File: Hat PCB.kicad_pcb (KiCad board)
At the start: 2 copper layers, 35 x 23 mm, 21 parts, among them J1 Batt, J2 Input 1, J3 USB4125-GF-A_REVA2, J4 ICSP, J5 Motor, Q1 AO3400A, SW1 SW_SPST, U1 INA333AIDGKR, U4 MCP73831-2-MC, U5 ATtiny13A-SS

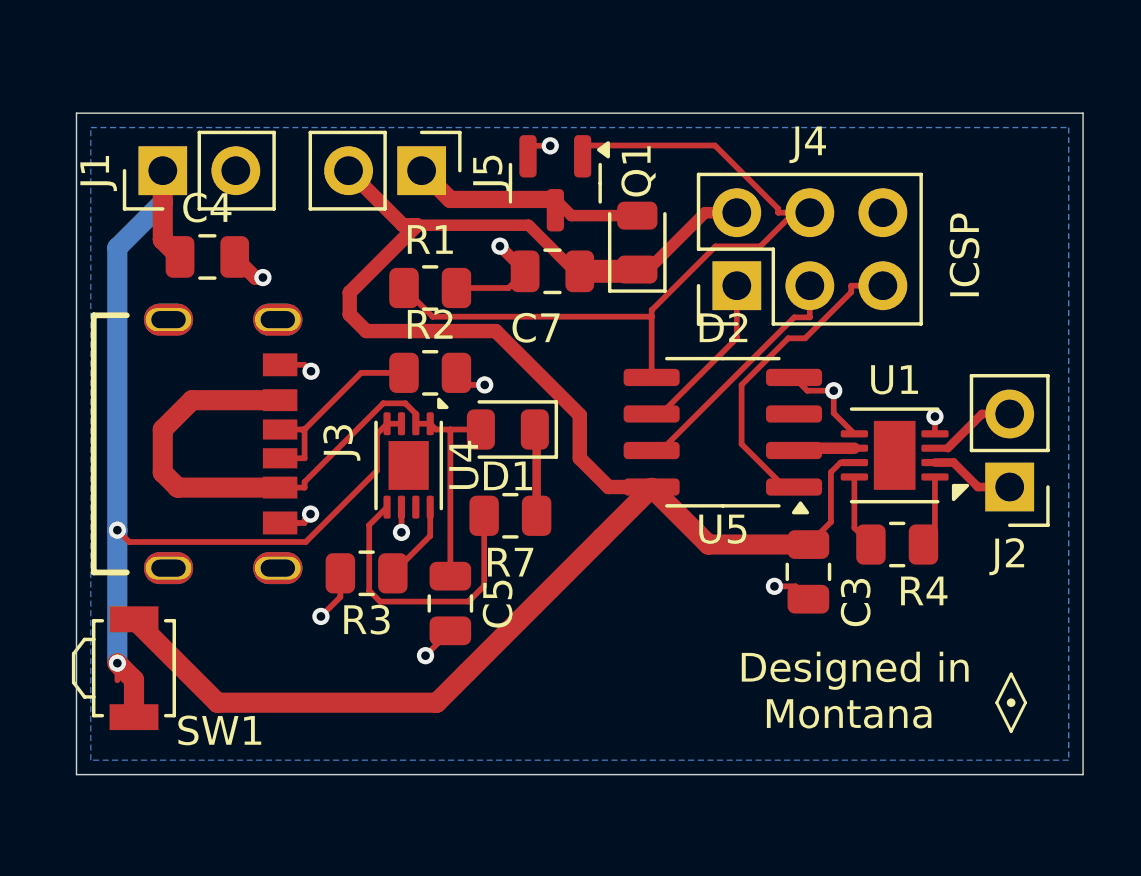
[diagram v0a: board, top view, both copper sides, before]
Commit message: widen traces
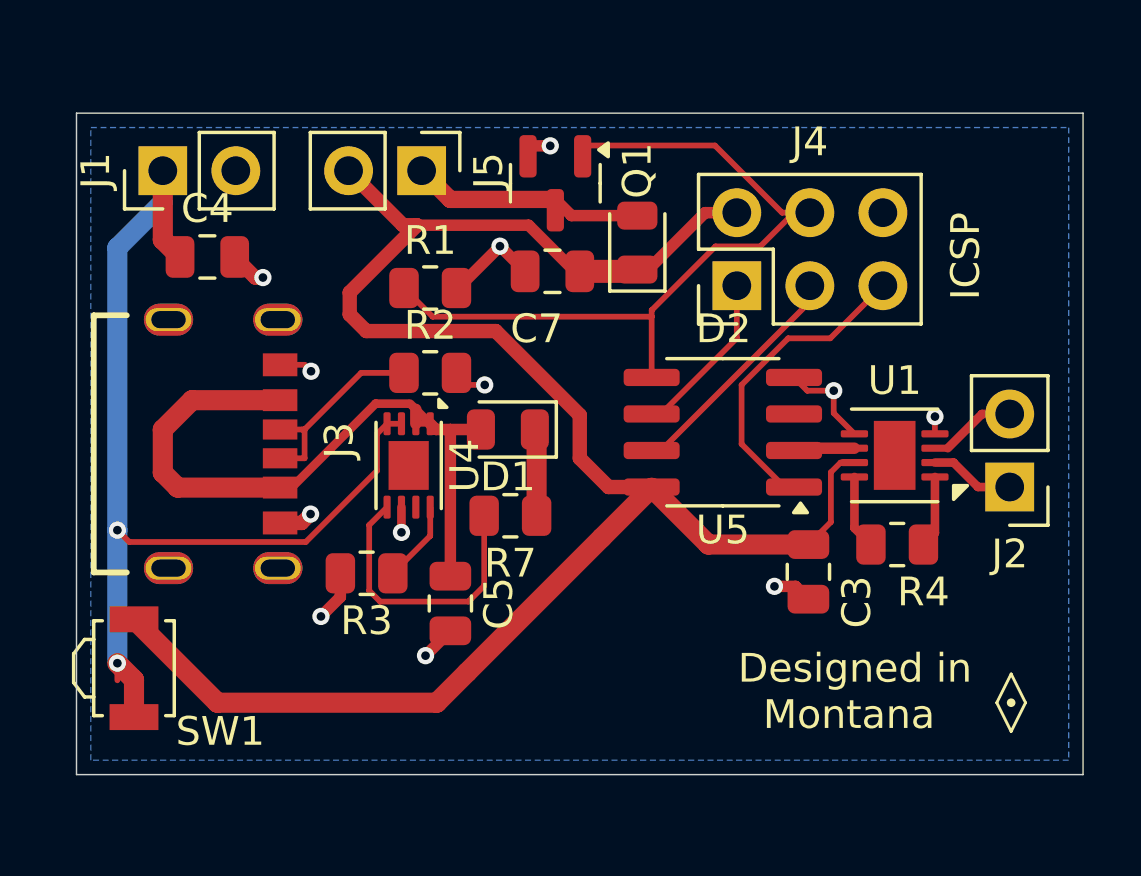
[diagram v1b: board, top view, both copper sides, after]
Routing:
- net VDD: track 24.3 -> 25.7 mm
- net GND: track 19.0 -> 18.4 mm

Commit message: new PCB design
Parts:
- added Q2: AO3400A, Package_TO_SOT_SMD:SOT-23, F.Cu at (218.1, 128.1)
- added R5: 11k, Resistor_SMD:R_0805_2012Metric, F.Cu at (214.1, 127.5)
- moved C5 9.39 mm to (224.5, 115.5), turned to 0 degrees
- moved R2 1.32 mm to (220.1, 116.0)
- moved R1 1.22 mm to (220.1, 113.5)
- moved C7 1.00 mm to (224.6, 113.0)
- moved U4 0.85 mm to (219.8, 119.5)
- moved R7 0.77 mm to (223.5, 121.0)
- moved D1 0.56 mm to (223.4, 118.5)
- moved SW1 0.54 mm to (210.5, 127.0)
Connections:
- C4 pad 1: Net-(J1-Pin_1) -> VBUS
- J1 pad 1: Net-(J1-Pin_1) -> VBUS
- SW1 pad 1: Net-(J1-Pin_1) -> Net-(Q2-S)
- U4 pad 3: Net-(J1-Pin_1) -> VBUS
- U4 pad 4: Net-(J1-Pin_1) -> VBUS
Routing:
- net Net-(J1-Pin_1): track 36.2 -> 0.00 mm, vias 2 -> 0
- net VBUS: track 0.00 -> 35.1 mm, vias 0 -> 4
- net VCC: track 68.6 -> 57.2 mm
- net Net-(Q2-G): track 9.98 -> 20.2 mm, vias 0 -> 2
- net Net-(Q2-S): track 0.00 -> 7.25 mm
- net VDD: track 25.7 -> 19.6 mm, vias 0 -> 2
- net Net-(J4-Pin_4): track 27.1 -> 30.7 mm, vias 0 -> 2
- net GND: track 18.4 -> 16.2 mm, vias 12 -> 15
- net Net-(J3-CC1): track 6.98 -> 6.13 mm
- net Net-(D1-K): track 3.03 -> 2.52 mm

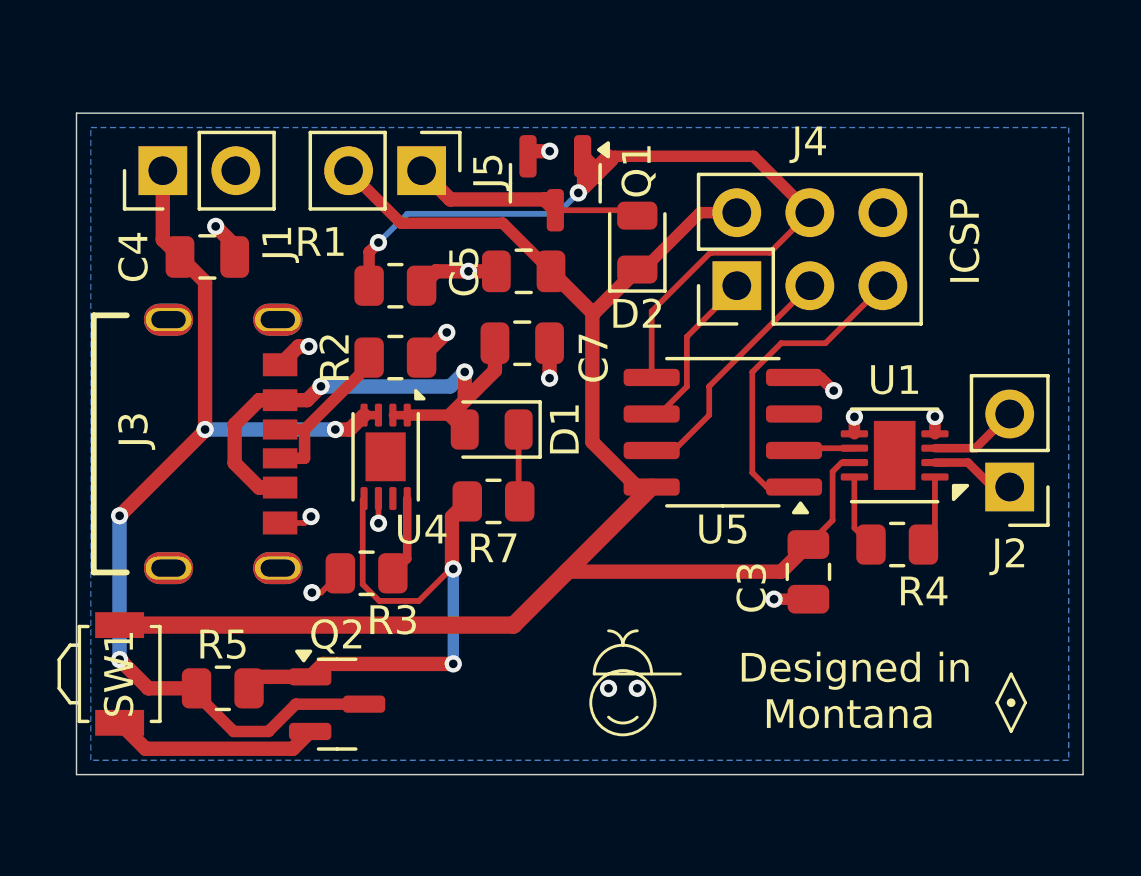
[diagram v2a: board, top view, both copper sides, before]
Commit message: improved connectors
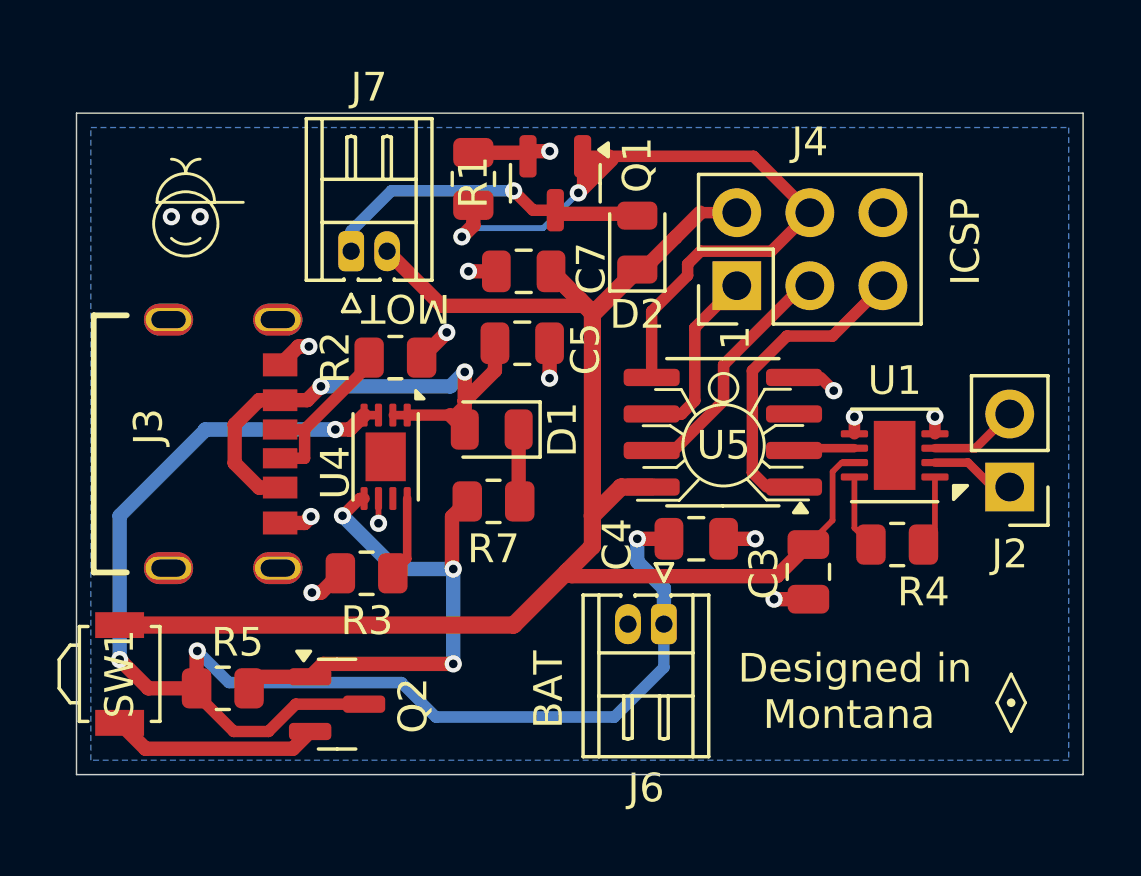
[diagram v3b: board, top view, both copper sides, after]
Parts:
- removed J1: Batt, Connector_PinHeader_2.54mm:PinHeader_1x02_P2.54mm_Vertical
- removed J5: Motor, Connector_PinHeader_2.54mm:PinHeader_1x02_P2.54mm_Vertical
- added J6: Conn_01x02 - Battery, Connector_Hirose:Hirose_DF13-02P-1.25DS_1x02_P1.25mm_Horizontal, F.Cu at (229.4, 125.3)
- added J7: Conn_01x02 - Motor, Connector_Hirose:Hirose_DF13-02P-1.25DS_1x02_P1.25mm_Horizontal, F.Cu at (218.6, 112.3)
- moved C4 19.6 mm to (230.6, 122.3)
- moved R1 4.60 mm to (222.8, 109.8), turned to 90 degrees
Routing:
- net VBUS: track 35.1 -> 50.7 mm
- net Net-(D2-A): track 8.15 -> 11.7 mm, vias 0 -> 1
- net Net-(Q2-G): track 20.2 -> 19.0 mm, vias 2 -> 3
- net Net-(J4-Pin_4): track 30.7 -> 29.6 mm
- net Net-(J4-Pin_1): track 5.85 -> 6.61 mm
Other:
- board text added: "1"
- board text added: "BAT"
- board text added: "MOT"

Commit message: add button
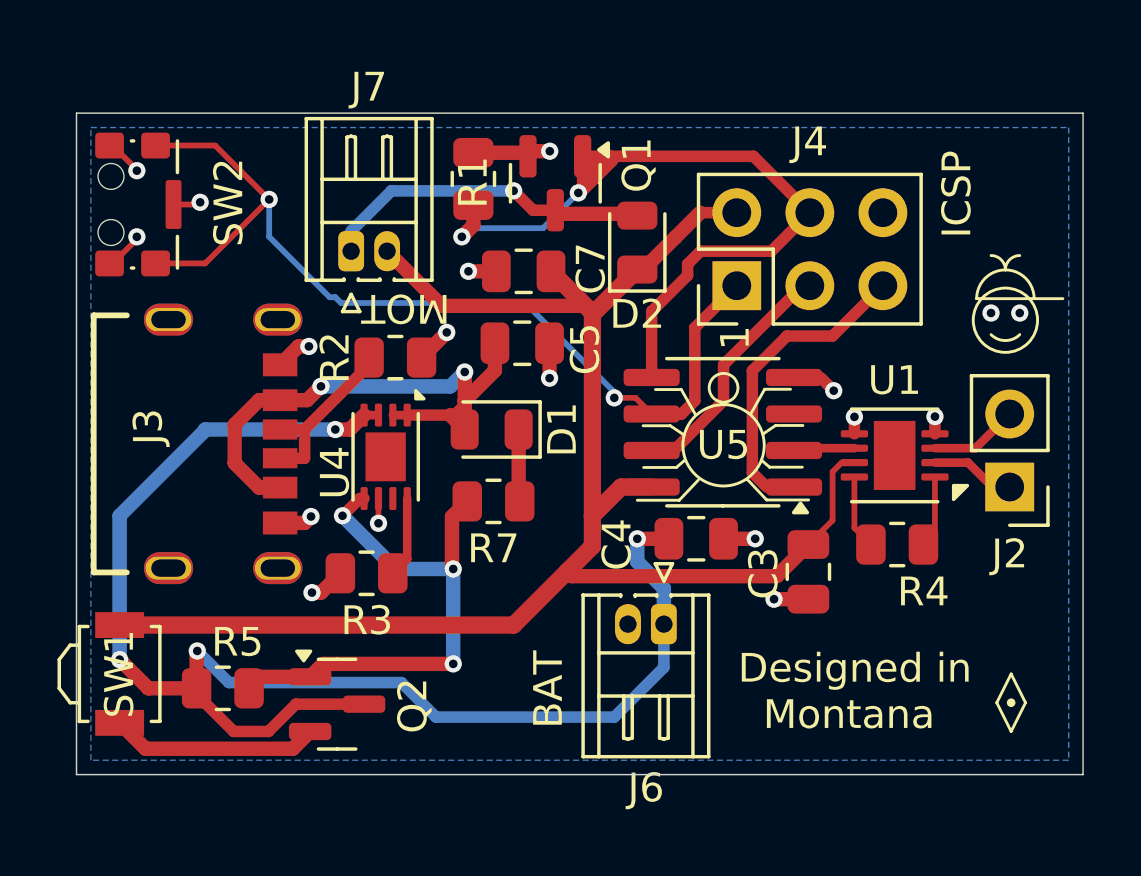
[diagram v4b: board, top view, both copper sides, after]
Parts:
- added SW2: CK_KMS2xxGP, Button_Switch_SMD:SW_SPST_CK_KMS2xxGP, F.Cu at (210.9, 110.7)
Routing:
- net Net-(J4-Pin_1): track 6.61 -> 33.5 mm, vias 0 -> 2
- net GND: track 16.2 -> 19.8 mm, vias 15 -> 18
